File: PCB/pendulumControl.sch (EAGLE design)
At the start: 25 parts, among them IC1 PIC32MX340F512H

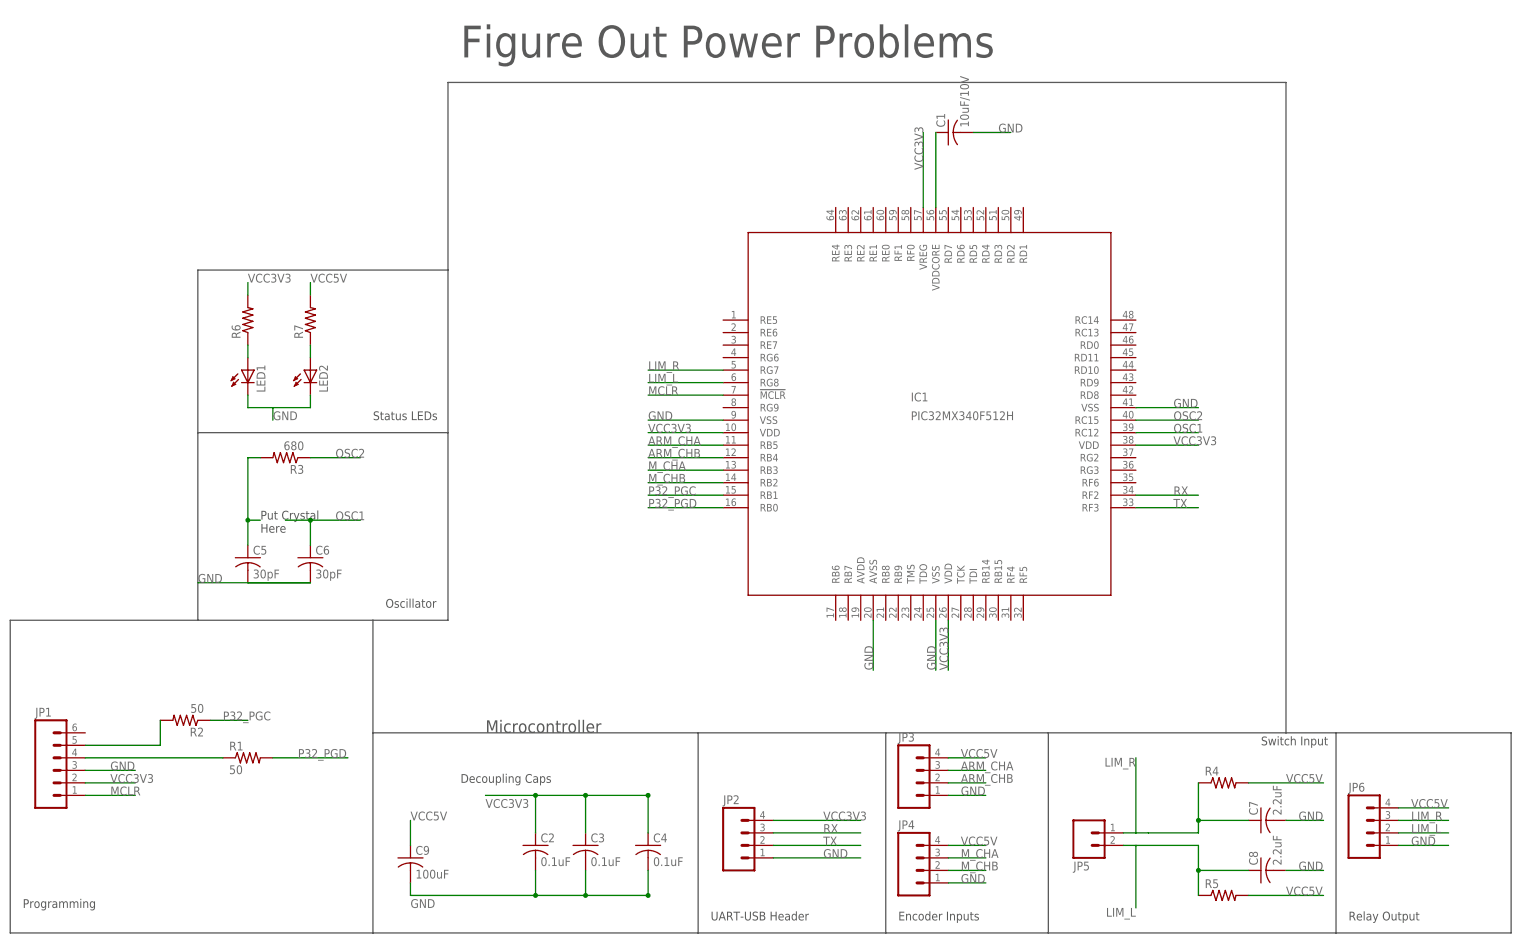
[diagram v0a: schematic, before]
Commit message: Added power input and regulation.
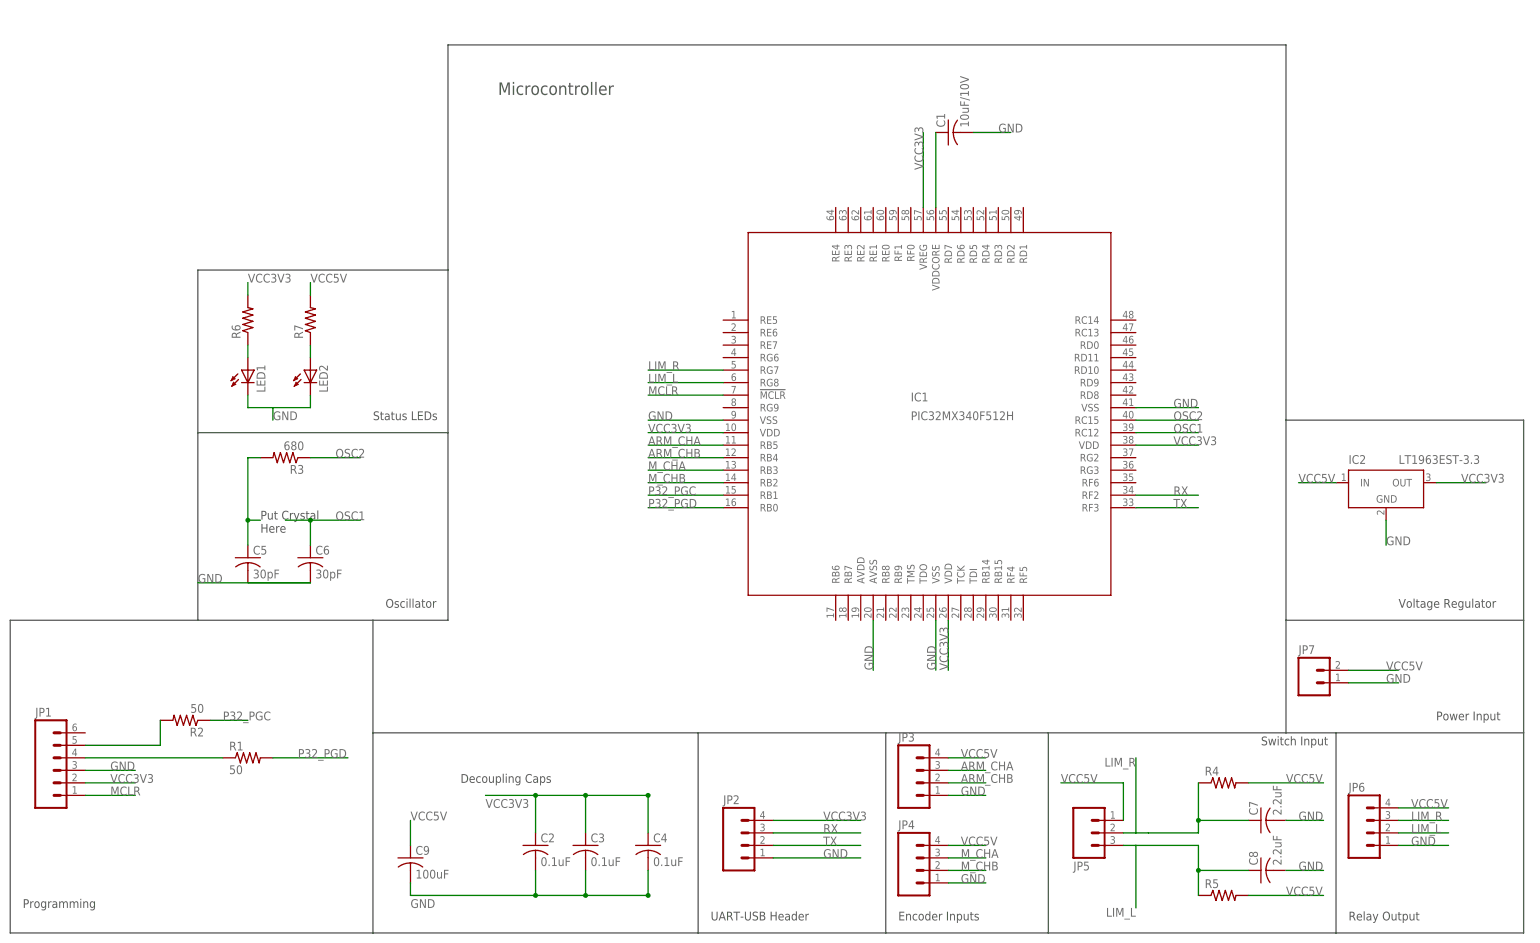
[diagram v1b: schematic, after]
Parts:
- added IC2: LT1963EST-3.3, linear-technology:LT1963EST-3.3
- added JP7: (no value), SparkFun-Connectors:M023.5MM
- JP5: device SparkFun-Connectors:M02PTH -> SparkFun-Connectors:M03PTH
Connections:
- net GND: now also IC2G$1.GND, JP7.1
- net LIM_L: now also JP5.3; no longer JP5.2
- net LIM_R: now also JP5.2; no longer JP5.1
- net VCC3V3: now also IC2G$1.OUT
- net VCC5V: now also IC2G$1.IN, JP5.1, JP7.2
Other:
- note added: "Power Input"
- note added: "Voltage Regulator"
- note removed: "Figure Out Power Problems"
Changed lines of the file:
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@@
 <layer number="56" name="wert" color="7" fill="1" visible="no" active="no"/>
 <layer number="57" name="tCAD" color="7" fill="1" visible="no" active="no"/>
+<layer number="59" name="tCarbon" color="7" fill="1" visible="no" active="no"/>
+<layer number="60" name="bCarbon" color="7" fill="1" visible="no" active="no"/>
 <layer number="90" name="Modules" color="5" fill="1" visible="yes" active="yes"/>
 <layer number="91" name="Nets" color="2" fill="1" visible="yes" active="yes"/>
@@
 <layer number="113" name="IDFDebug" color="4" fill="1" visible="yes" active="yes"/>
 <layer number="116" name="Patch_BOT" color="9" fill="4" visible="yes" active="yes"/>
+<layer number="118" name="Rect_Pads" color="7" fill="1" visible="no" active="yes"/>
 <layer number="121" name="_tsilk" color="7" fill="1" visible="yes" active="yes"/>
 <layer number="122" name="_bsilk" color="7" fill="1" visible="yes" active="yes"/>
@@
 <layer number="127" name="_tValues" color="7" fill="1" visible="yes" active="yes"/>
 <layer number="128" name="_bValues" color="7" fill="1" visible="yes" active="yes"/>
+<layer number="129" name="Mask" color="7" fill="1" visible="no" active="yes"/>
 <layer number="131" name="tAdjust" color="7" fill="1" visible="yes" active="yes"/>
 <layer number="132" name="bAdjust" color="7" fill="1" visible="yes" active="yes"/>
@@
 <layer number="223" name="223bmp" color="24" fill="1" visible="no" active="no"/>
 <layer number="224" name="224bmp" color="25" fill="1" visible="no" active="no"/>
+<layer number="225" name="225bmp" color="7" fill="1" visible="no" active="yes"/>
+<layer number="226" name="226bmp" color="7" fill="1" visible="no" active="yes"/>
+<layer number="227" name="227bmp" color="7" fill="1" visible="no" active="yes"/>
+<layer number="228" name="228bmp" color="7" fill="1" visible="no" active="yes"/>
+<layer number="229" name="229bmp" color="7" fill="1" visible="no" active="yes"/>
+<layer number="230" name="230bmp" color="7" fill="1" visible="no" active="yes"/>
+<layer number="231" name="231bmp" color="7" fill="1" visible="no" active="yes"/>
 <layer number="248" name="Housing" color="7" fill="1" visible="yes" active="yes"/>
 <layer number="249" name="Edge" color="7" fill="1" visible="yes" active="yes"/>
@@
 <layer number="251" name="SMDround" color="12" fill="11" visible="no" active="no"/>
 <layer number="254" name="cooling" color="7" fill="1" visible="yes" active="yes"/>
+<layer number="255" name="routoute" color="7" fill="1" visible="no" active="yes"/>
 </layers>
 <schematic xreflabel="%F%N/%S.%C%R" xrefpart="/%S.%C%R">
@@
 <part name="JP3" library="SparkFun-Connectors" deviceset="M04" device="PTH"/>
 <part name="JP4" library="SparkFun-Connectors" deviceset="M04" device="PTH"/>
-<part name="JP5" library="SparkFun-Connectors" deviceset="M02" device="PTH"/>
+<part name="JP5" library="SparkFun-Connectors" deviceset="M03" device="PTH"/>
 <part name="R4" library="rcl" deviceset="R-US_" device="R0805"/>
 <part name="R5" library="rcl" deviceset="R-US_" device="R0805"/>
@@
 <part name="R6" library="rcl" deviceset="R-US_" device="R0805"/>
 <part name="R7" library="rcl" deviceset="R-US_" device="R0805"/>
+<part name="JP7" library="SparkFun-Connectors" deviceset="M02" device="3.5MM"/>
+<part name="IC2" library="linear-technology" deviceset="LT1963EST" device="" technology="-3.3"/>
 </parts>
 <sheets>
 <sheet>
 <plain>
-<wire x1="-22.86" y1="104.14" x2="-22.86" y2="66.04" width="0.1524" layer="97"/>
+<wire x1="-22.86" y1="111.76" x2="-22.86" y2="66.04" width="0.1524" layer="97"/>
 <wire x1="-22.86" y1="66.04" x2="-22.86" y2="33.02" width="0.1524" layer="97"/>
 <wire x1="-22.86" y1="33.02" x2="-22.86" y2="-5.08" width="0.1524" layer="97"/>
@@
 <wire x1="66.04" y1="-68.58" x2="99.06" y2="-68.58" width="0.1524" layer="97"/>
 <wire x1="99.06" y1="-68.58" x2="157.48" y2="-68.58" width="0.1524" layer="97"/>
-<wire x1="157.48" y1="-68.58" x2="193.04" y2="-68.58" width="0.1524" layer="97"/>
+<wire x1="157.48" y1="-68.58" x2="195.58" y2="-68.58" width="0.1524" layer="97"/>
 <wire x1="-38.1" y1="-5.08" x2="-73.66" y2="-5.08" width="0.1524" layer="97"/>
 <wire x1="-73.66" y1="-5.08" x2="-111.76" y2="-5.08" width="0.1524" layer="97"/>
@@
 <wire x1="66.04" y1="-27.94" x2="66.04" y2="-68.58" width="0.1524" layer="97"/>
 <text x="30.48" y="-66.04" size="1.778" layer="97">UART-USB Header</text>
-<text x="-20.32" y="109.22" size="6.4516" layer="97">Figure Out Power Problems</text>
 <wire x1="66.04" y1="-27.94" x2="99.06" y2="-27.94" width="0.1524" layer="97"/>
 <wire x1="99.06" y1="-27.94" x2="99.06" y2="-68.58" width="0.1524" layer="97"/>
@@
 <text x="142.24" y="-30.48" size="1.778" layer="97">Switch Input</text>
 <text x="160.02" y="-66.04" size="1.778" layer="97">Relay Output</text>
-<wire x1="157.48" y1="-27.94" x2="193.04" y2="-27.94" width="0.1524" layer="97"/>
-<wire x1="193.04" y1="-27.94" x2="193.04" y2="-68.58" width="0.1524" layer="97"/>
-<wire x1="-22.86" y1="104.14" x2="147.32" y2="104.14" width="0.1524" layer="97"/>
-<wire x1="147.32" y1="104.14" x2="147.32" y2="-27.94" width="0.1524" layer="97"/>
-<text x="-15.24" y="-27.94" size="2.54" layer="97">Microcontroller</text>
+<wire x1="157.48" y1="-27.94" x2="195.58" y2="-27.94" width="0.1524" layer="97"/>
+<wire x1="195.58" y1="-27.94" x2="195.58" y2="-68.58" width="0.1524" layer="97"/>
+<wire x1="-22.86" y1="111.76" x2="147.32" y2="111.76" width="0.1524" layer="97"/>
+<wire x1="147.32" y1="111.76" x2="147.32" y2="35.56" width="0.1524" layer="97"/>
+<text x="-12.7" y="101.6" size="2.54" layer="97">Microcontroller</text>
+<wire x1="147.32" y1="35.56" x2="147.32" y2="-5.08" width="0.1524" layer="97"/>
+<wire x1="147.32" y1="-5.08" x2="147.32" y2="-27.94" width="0.1524" layer="97"/>
 <wire x1="-73.66" y1="33.02" x2="-73.66" y2="66.04" width="0.1524" layer="97"/>
 <wire x1="-73.66" y1="66.04" x2="-22.86" y2="66.04" width="0.1524" layer="97"/>
 <text x="-38.1" y="35.56" size="1.778" layer="97">Status LEDs</text>
+<wire x1="147.32" y1="35.56" x2="195.58" y2="35.56" width="0.1524" layer="97"/>
+<wire x1="195.58" y1="35.56" x2="195.58" y2="-5.08" width="0.1524" layer="97"/>
+<text x="177.8" y="-25.4" size="1.778" layer="97">Power Input</text>
+<wire x1="195.58" y1="-5.08" x2="195.58" y2="-27.94" width="0.1524" layer="97"/>
+<wire x1="147.32" y1="-5.08" x2="195.58" y2="-5.08" width="0.1524" layer="97"/>
+<text x="170.18" y="-2.54" size="1.778" layer="97">Voltage Regulator</text>
 </plain>
 <instances>
@@
 <instance part="R6" gate="G$1" x="-63.5" y="55.88" rot="R90"/>
 <instance part="R7" gate="G$1" x="-50.8" y="55.88" rot="R90"/>
+<instance part="JP7" gate="G$1" x="152.4" y="-17.78"/>
+<instance part="IC2" gate="G$1" x="167.64" y="20.32"/>
 </instances>
 <busses>
@@
 <label x="-58.42" y="35.56" size="1.778" layer="97"/>
 </segment>
+<segment>
+<pinref part="JP7" gate="G$1" pin="1"/>
+<wire x1="160.02" y1="-17.78" x2="170.18" y2="-17.78" width="0.1524" layer="91"/>
+<label x="167.64" y="-17.78" size="1.778" layer="95"/>
+</segment>
+<segment>
+<pinref part="IC2" gate="G$1" pin="GND"/>
+<wire x1="167.64" y1="15.24" x2="167.64" y2="10.16" width="0.1524" layer="91"/>
+<label x="167.64" y="10.16" size="1.778" layer="95"/>
+</segment>
 </net>
 <net name="VCC3V3" class="0">
@@
 <label x="-63.5" y="63.5" size="1.778" layer="97"/>
 </segment>
+<segment>
+<pinref part="IC2" gate="G$1" pin="OUT"/>
+<wire x1="177.8" y1="22.86" x2="187.96" y2="22.86" width="0.1524" layer="91"/>
+<label x="182.88" y="22.86" size="1.778" layer="95"/>
+</segment>
 </net>
 <net name="N$10" class="0">
@@
 </segment>
 <segment>
-<pinref part="JP5" gate="G$1" pin="1"/>
+<pinref part="JP5" gate="G$1" pin="2"/>
 <wire x1="114.3" y1="-48.26" x2="116.84" y2="-48.26" width="0.1524" layer="91"/>
 <pinref part="R4" gate="G$1" pin="1"/>
@@
 </segment>
 <segment>
-<pinref part="JP5" gate="G$1" pin="2"/>
+<pinref part="JP5" gate="G$1" pin="3"/>
 <wire x1="114.3" y1="-50.8" x2="116.84" y2="-50.8" width="0.1524" layer="91"/>
 <pinref part="R5" gate="G$1" pin="1"/>
@@
 <label x="-50.8" y="63.5" size="1.778" layer="97"/>
 </segment>
-</net>
+<segment>
+<pinref part="JP7" gate="G$1" pin="2"/>
+<wire x1="160.02" y1="-15.24" x2="170.18" y2="-15.24" width="0.1524" layer="91"/>
+<label x="167.64" y="-15.24" size="1.778" layer="95"/>
+</segment>
+<segment>
+<pinref part="IC2" gate="G$1" pin="IN"/>
+<wire x1="157.48" y1="22.86" x2="149.86" y2="22.86" width="0.1524" layer="91"/>
+<label x="149.86" y="22.86" size="1.778" layer="95"/>
+</segment>
+<segment>
+<pinref part="JP5" gate="G$1" pin="1"/>
+<wire x1="114.3" y1="-45.72" x2="114.3" y2="-38.1" width="0.1524" layer="91"/>
+<wire x1="114.3" y1="-38.1" x2="101.6" y2="-38.1" width="0.1524" layer="91"/>
+<label x="101.6" y="-38.1" size="1.778" layer="95"/>
+</segment>
+</net>
